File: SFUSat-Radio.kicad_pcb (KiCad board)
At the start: 4 copper layers, 95.9 x 90.2 mm, 284 parts, among them J1 PC104-8BIT, J10 TP_TH_150, J11 TP_TH_150, J12 SMA, J13 SMA, J14 SMA, J15 Conn_01x02, J16 SMA, J17 SMA, J18 SMA, J19 Conn_01x03, J2 PC104PTH, J20 Conn_01x03, J21 TP_TH_150, J22 TP_TH_150, J23 TP_TH_150, J24 TP_TH_150, J25 Conn_01x02, J3 PC104PTH, J4 PC104PTH, J400 SMA, J401 TP_TH_150, J402 TP_TH_150, J404 TP_TH_150, J405 TP_TH_150, J406 TP_TH_150, J5 PC104PTH, J500 SMA, J501 TP_TH_150, J502 TP_TH_150, J504 TP_TH_150, J505 TP_TH_150, J506 TP_TH_150, J6 SMA, J7 TP_TH_150, J8 TP_TH_150, J9 TP_TH_150, P1 3pin-DC-power, U1 SINGLE_0402, U10 TPS799, U100 CC1101-Q1, U101 0433BM15A0001, U11 SINGLE_0402, U110 CC1101-Q1, U111 0915BM15A0001E, U12 CONN_02X05_SHRD, U13 CONN_02X05_SHRD, U14 2N7002DW, U15 TPS62175DQCR, U16 TPS71750DSER, U17 74LVC1G14SE-7, U2 SKY13345-368LF, U3 CD4555BPWR, U4 LMS3635AQRNLRQ1, U400 SINGLE_0402, U401 LMV358, U402 RF6886, U420 2N7002DW, U5 MML09211H, U500 SINGLE_0402, U501 LMV358, U502 RF6886, U6 SINGLE_0402, U600 STLM75, U610 STLM75, U7 SKY13372-467LF, U8 SINGLE_0402, U9 TLV702, X100 NX3225GA, X110 NX3225GA

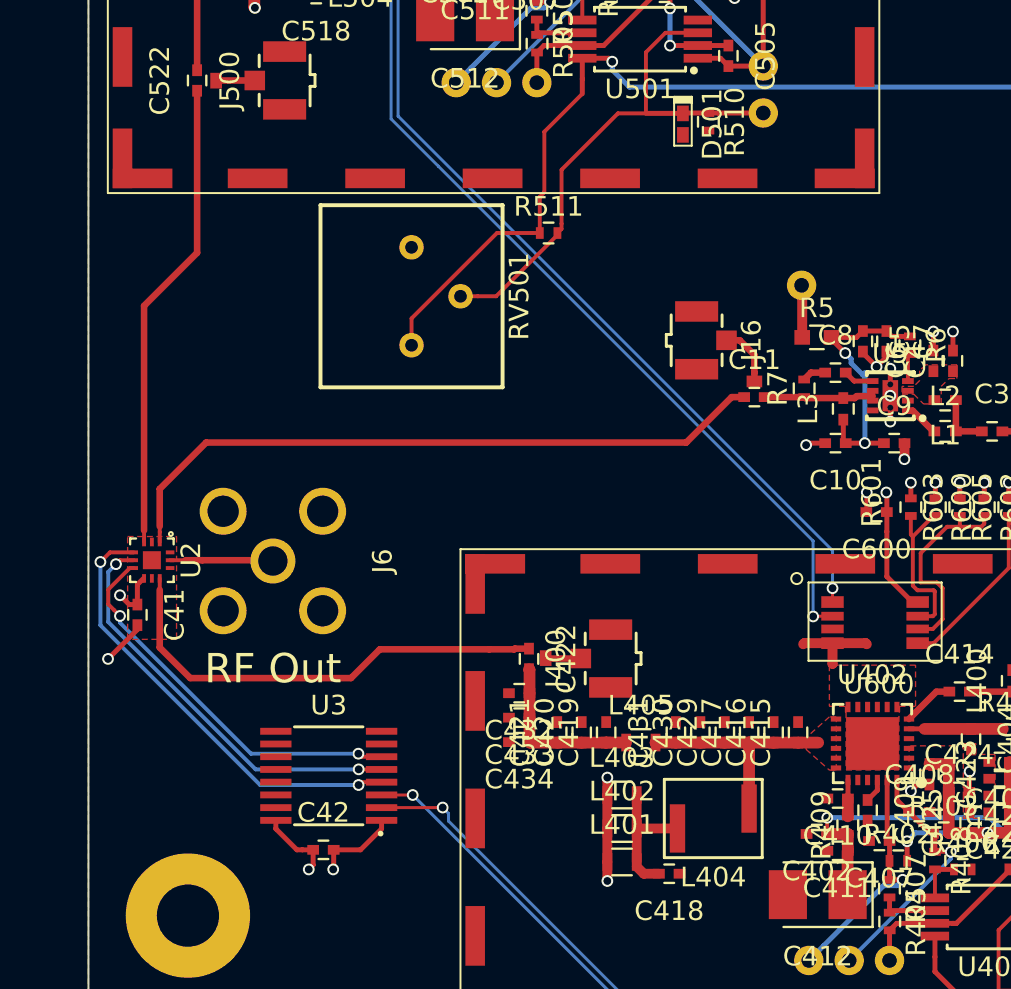
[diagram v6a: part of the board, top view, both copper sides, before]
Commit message: More power plane routing
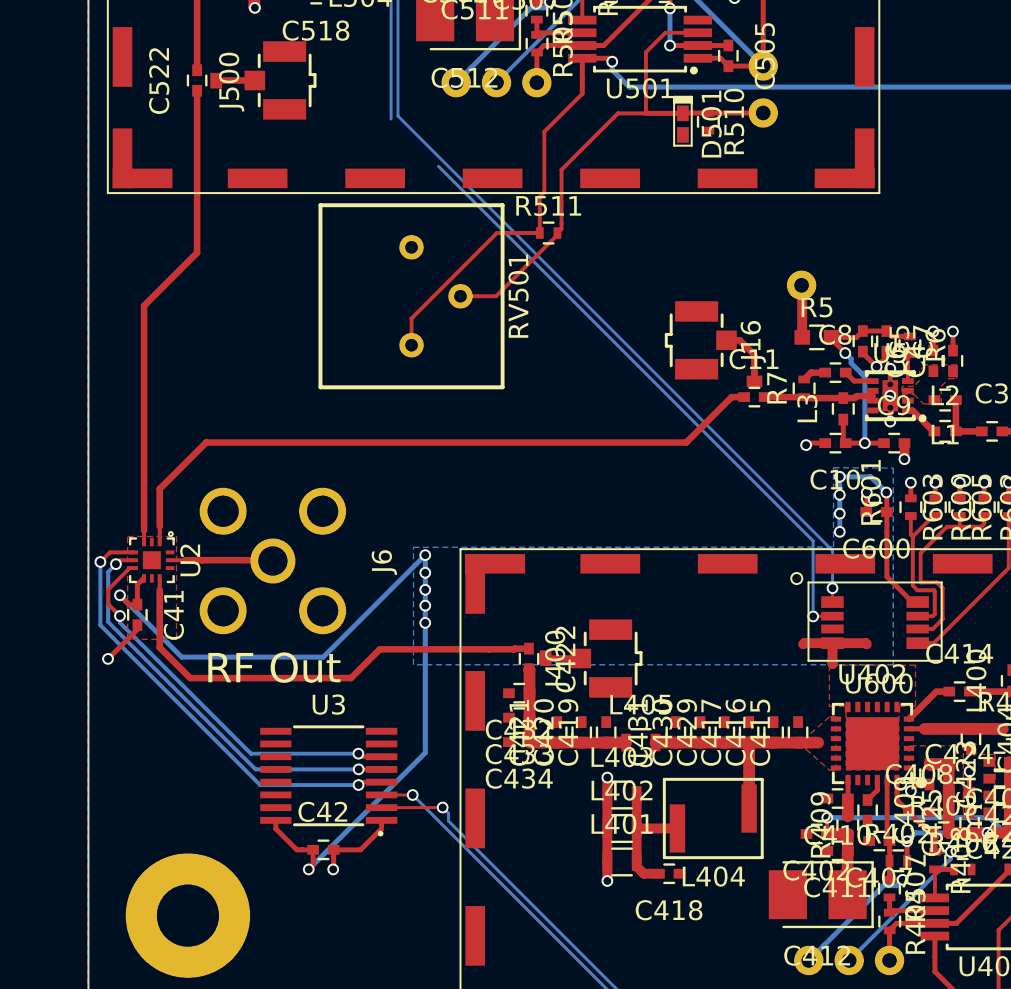
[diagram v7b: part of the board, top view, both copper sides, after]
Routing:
- net /3V3: track 41.3 -> 84.4 mm, vias 18 -> 27
- net /SCL: track 61.7 -> 58.2 mm
- added copper zone on B.Cu, net /3V3
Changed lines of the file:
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@@
   (general
     (links 732)
-    (no_connects 67)
+    (no_connects 66)
     (area 45.1 57.330476 358.142847 159.700001)
     (thickness 1.6)
     (drawings 26)
-    (tracks 1294)
+    (tracks 1317)
     (zones 0)
     (modules 284)
@@
   (segment (start 180.12 109.73) (end 180.14 109.71) (width 0.336) (layer F.Cu) (net 65))
   (segment (start 180.12 114.865) (end 180.14 114.885) (width 0.254) (layer F.Cu) (net 65))
+  (segment (start 150.87 119.08) (end 150.87 120.01) (width 0.254) (layer B.Cu) (net 66))
+  (via (at 150.87 120.01) (size 0.6) (drill 0.4) (layers F.Cu B.Cu) (net 66))
+  (segment (start 150.87 118.12) (end 150.87 119.08) (width 0.254) (layer B.Cu) (net 66))
+  (via (at 150.87 119.08) (size 0.6) (drill 0.4) (layers F.Cu B.Cu) (net 66))
+  (segment (start 150.87 117.2) (end 150.87 118.12) (width 0.254) (layer B.Cu) (net 66))
+  (via (at 150.87 118.12) (size 0.6) (drill 0.4) (layers F.Cu B.Cu) (net 66))
+  (segment (start 152.45 117.2) (end 150.87 117.2) (width 0.254) (layer B.Cu) (net 66))
+  (via (at 150.87 117.2) (size 0.6) (drill 0.4) (layers F.Cu B.Cu) (net 66))
+  (segment (start 153.25 118) (end 152.45 117.2) (width 0.254) (layer B.Cu) (net 66))
+  (segment (start 152.45 117.2) (end 152.377962 117.2) (width 0.254) (layer B.Cu) (net 66))
+  (segment (start 123.75 137.25) (end 129.7 131.3) (width 0.254) (layer B.Cu) (net 66))
+  (segment (start 129.7 131.3) (end 129.7 124.66) (width 0.254) (layer B.Cu) (net 66))
+  (segment (start 129.7 123.78) (end 129.7 124.66) (width 0.254) (layer B.Cu) (net 66))
+  (via (at 129.7 124.66) (size 0.6) (drill 0.4) (layers F.Cu B.Cu) (net 66))
+  (segment (start 129.7 122.97) (end 129.7 123.78) (width 0.254) (layer B.Cu) (net 66))
+  (via (at 129.7 123.78) (size 0.6) (drill 0.4) (layers F.Cu B.Cu) (net 66))
+  (segment (start 129.7 122.97) (end 129.7 122.1) (width 0.254) (layer B.Cu) (net 66))
+  (segment (start 129.7 121.2) (end 129.7 122.1) (width 0.254) (layer B.Cu) (net 66))
+  (via (at 129.7 122.1) (size 0.6) (drill 0.4) (layers F.Cu B.Cu) (net 66))
+  (via (at 129.7 122.97) (size 0.6) (drill 0.4) (layers F.Cu B.Cu) (net 66))
+  (segment (start 117.27001 126.41) (end 124.49 126.41) (width 0.254) (layer B.Cu) (net 66))
+  (segment (start 124.49 126.41) (end 129.7 121.2) (width 0.254) (layer B.Cu) (net 66))
+  (via (at 129.7 121.2) (size 0.6) (drill 0.4) (layers F.Cu B.Cu) (net 66))
+  (segment (start 114.11001 123.25) (end 117.27001 126.41) (width 0.254) (layer B.Cu) (net 66))
   (segment (start 191.55 101.25) (end 191.55 102.03) (width 0.508) (layer F.Cu) (net 66))
   (via (at 191.55 102.03) (size 0.6) (drill 0.4) (layers F.Cu B.Cu) (net 66))
@@
   (segment (start 144.16 98.62) (end 142.88 98.62) (width 0.254) (layer F.Cu) (net 108))
   (segment (start 142.88 98.62) (end 142.86 98.64) (width 0.254) (layer F.Cu) (net 108))
+  (segment (start 149.51 120.478382) (end 130.375809 101.344191) (width 0.1524) (layer B.Cu) (net 109))
+  (segment (start 149.51 124.33) (end 149.51 120.478382) (width 0.1524) (layer B.Cu) (net 109))
+  (via (at 149.51 124.33) (size 0.6) (drill 0.4) (layers F.Cu B.Cu) (net 109))
+  (segment (start 150.497844 124.32) (end 149.52 124.32) (width 0.1524) (layer F.Cu) (net 109))
+  (segment (start 149.52 124.32) (end 149.51 124.33) (width 0.1524) (layer F.Cu) (net 109))
   (segment (start 129.24 79.72) (end 132.32 79.72) (width 0.1524) (layer F.Cu) (net 109))
   (segment (start 132.32 79.72) (end 132.325 79.725) (width 0.1524) (layer F.Cu) (net 109))
@@
   (segment (start 127.95759 81.00241) (end 129.24 79.72) (width 0.1524) (layer B.Cu) (net 109))
   (via (at 129.24 79.72) (size 0.6) (drill 0.4) (layers F.Cu B.Cu) (net 109))
-  (segment (start 130.375809 101.344191) (end 127.95759 98.925973) (width 0.1524) (layer B.Cu) (net 109))
-  (segment (start 149.51 120.478382) (end 130.375809 101.344191) (width 0.1524) (layer B.Cu) (net 109))
-  (segment (start 149.51 124.33) (end 149.51 120.478382) (width 0.1524) (layer B.Cu) (net 109))
-  (segment (start 150.497844 124.32) (end 149.52 124.32) (width 0.1524) (layer F.Cu) (net 109))
-  (segment (start 149.52 124.32) (end 149.51 124.33) (width 0.1524) (layer F.Cu) (net 109))
-  (via (at 149.51 124.33) (size 0.6) (drill 0.4) (layers F.Cu B.Cu) (net 109))
   (segment (start 195.69 98.97) (end 192.88 98.97) (width 0.2) (layer F.Cu) (net 109))
   (segment (start 192.88 98.97) (end 192.45 99.4) (width 0.2) (layer F.Cu) (net 109))
   (segment (start 192.45 99.4) (end 192.45 99.5) (width 0.2) (layer F.Cu) (net 109))
-  (segment (start 150.5 122.89) (end 150.5 123.592844) (width 0.1524) (layer F.Cu) (net 110))
-  (segment (start 150.5 123.592844) (end 150.497844 123.595) (width 0.1524) (layer F.Cu) (net 110))
   (segment (start 128.31 98.78) (end 150.5 120.97) (width 0.1524) (layer B.Cu) (net 110))
   (segment (start 150.5 120.97) (end 150.5 122.89) (width 0.1524) (layer B.Cu) (net 110))
   (via (at 150.5 122.89) (size 0.6) (drill 0.4) (layers F.Cu B.Cu) (net 110))
+  (segment (start 150.5 122.89) (end 150.5 123.592844) (width 0.1524) (layer F.Cu) (net 110))
+  (segment (start 150.5 123.592844) (end 150.497844 123.595) (width 0.1524) (layer F.Cu) (net 110))
   (segment (start 128.31 81.645736) (end 128.31 98.78) (width 0.1524) (layer B.Cu) (net 110))
   (segment (start 131.38 79) (end 130.955736 79) (width 0.1524) (layer B.Cu) (net 110))
@@
     (polygon
       (pts
-        (xy 114 76) (xy 114 103) (xy 153 103) (xy 153 76)
-      )
-    )
-  )
-  (zone (net 78) (net_name /3V6) (layer PWR.Cu) (hatch full 0.508)
-    (priority 1)
-    (connect_pads yes (clearance 0.2))
-    (min_thickness 0.2)
-    (fill yes (arc_segments 16) (thermal_gap 0.127) (thermal_bridge_width 0.26))
-    (polygon
-      (pts
-        (xy 131.576926 121) (xy 131.576926 148) (xy 170.576926 148) (xy 170.576926 121)
+        (xy 153 106.25) (xy 147.5 106.25) (xy 147.5 121) (xy 170.576926 121) (xy 170.576926 148)
+        (xy 131.576926 148) (xy 131.576926 121) (xy 131.58 121) (xy 131.6 103) (xy 114 103)
+        (xy 114 76) (xy 153 76)
       )
     )
@@
       )
     )
+  )
+  (zone (net 66) (net_name /3V3) (layer B.Cu) (hatch edge 0.508)
+    (priority 1)
+    (connect_pads yes (clearance 0.154))
+    (min_thickness 0.254)
+    (fill yes (arc_segments 16) (thermal_gap 0.508) (thermal_bridge_width 0.508))
+    (polygon
+      (pts
+        (xy 153.6 116.75) (xy 153.6 126.8) (xy 129.1 126.8) (xy 129.1 120.8) (xy 150.55 120.79)
+        (xy 150.55 116.74)
+      )
+    )
